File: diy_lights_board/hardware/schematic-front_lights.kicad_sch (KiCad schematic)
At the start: 21 parts, among them Q1 BSP171, Q2 BSP171, Q3 BSP171, Q4 BSP171, Q5 FDV301, Q6 FDV301, Q7 FDV301, Q8 FDV301, Q9 FDV301, U1 Step-down converter to 3.3V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

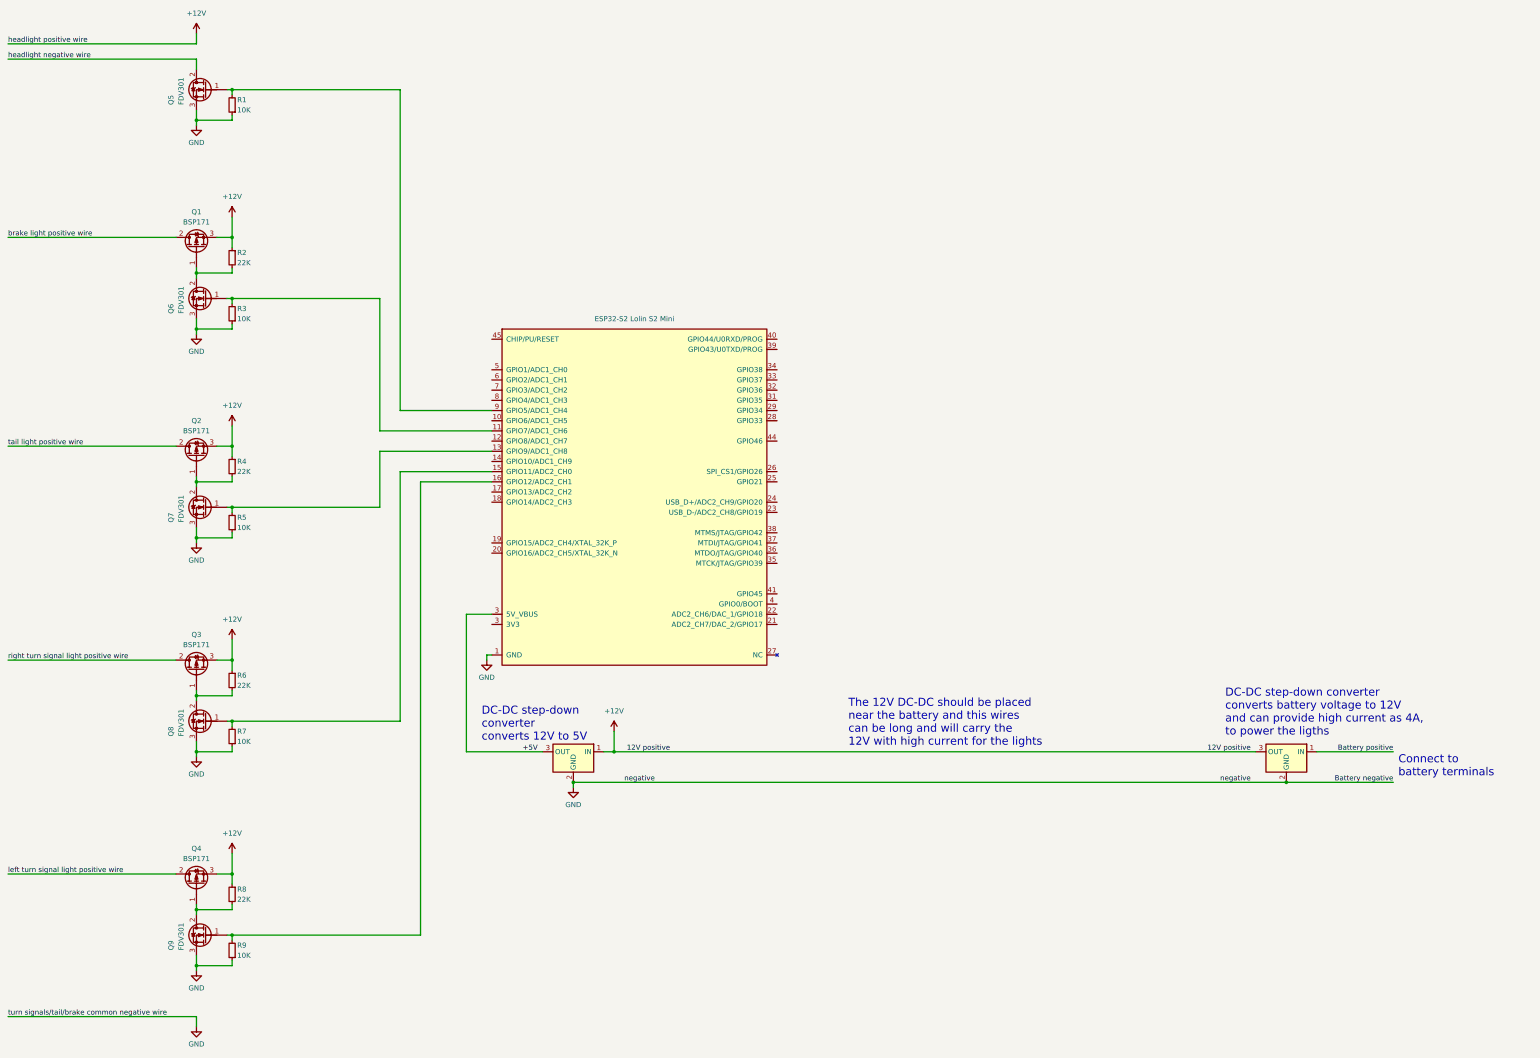
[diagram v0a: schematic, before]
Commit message: Did finish the front and rear lights boards
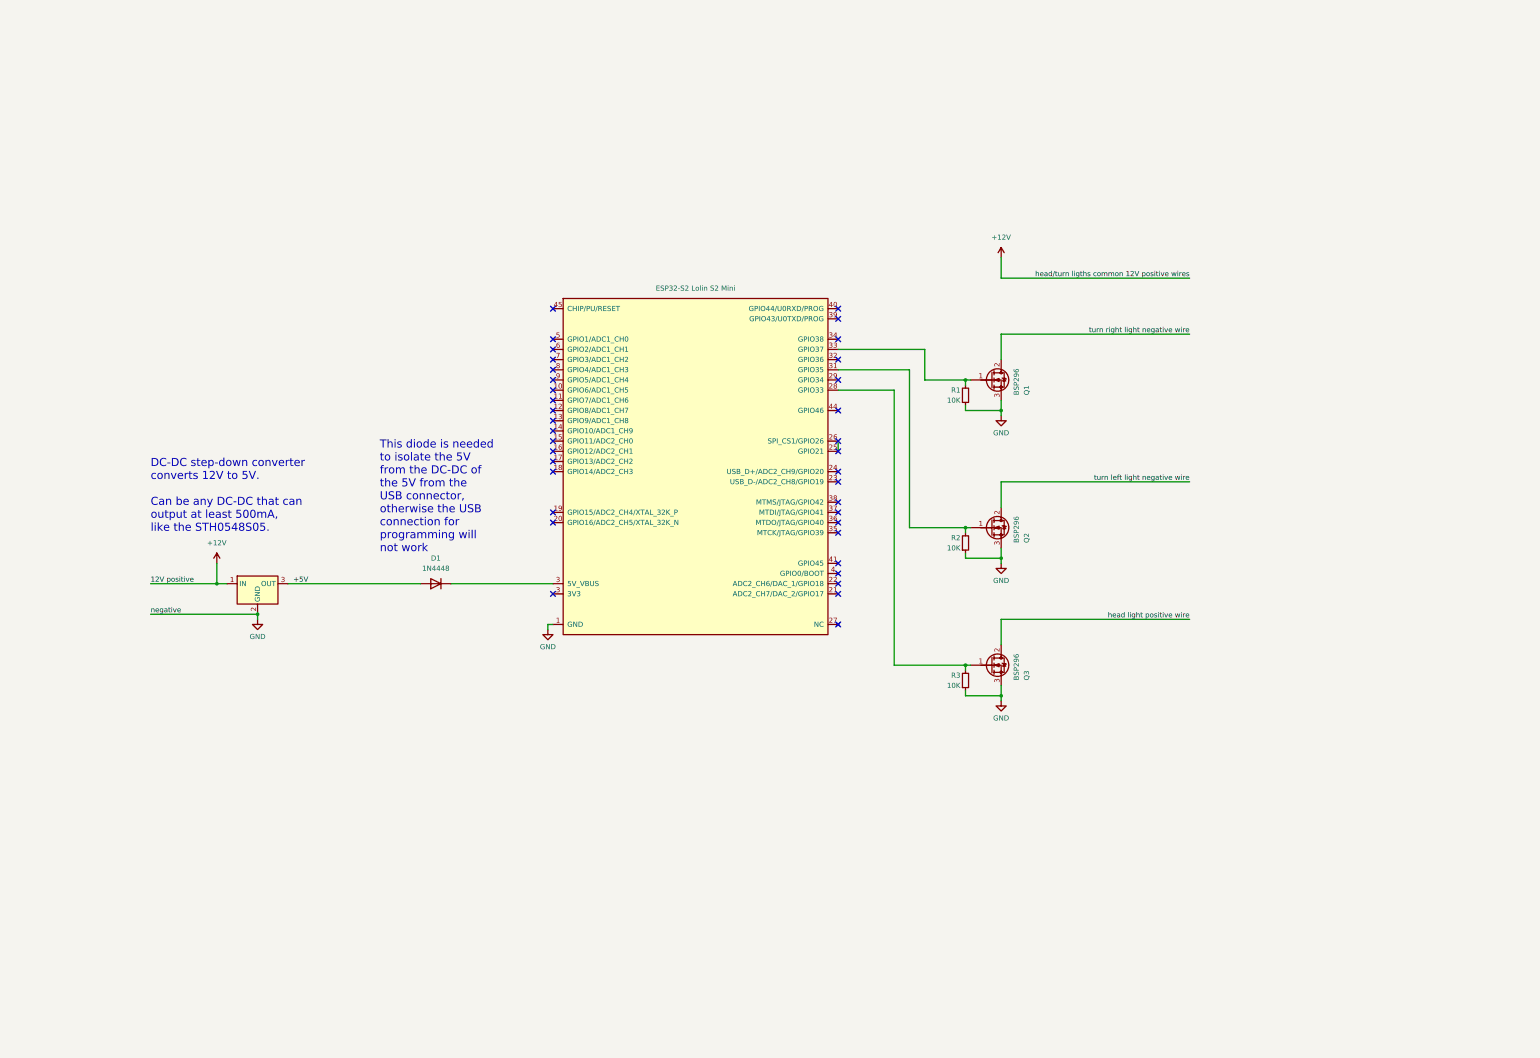
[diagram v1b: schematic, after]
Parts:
- removed Q1, Q2, Q3, Q4: BSP171, Package_TO_SOT_THT:TO-220-3_Vertical, symbol Transistor_FET:IRF9540N
- removed Q5, Q6, Q7, Q8, Q9: FDV301, Package_TO_SOT_SMD:SOT-223-3_TabPin2, symbol Transistor_FET:BSP129
- removed R4, R6, R8: 22K, symbol Device:R_Small
- removed R5, R7, R9: 10K, symbol Device:R_Small
- removed U3: Step-down converter to 3.3V, Converter_DCDC:Converter_DCDC_Murata_OKI-78SR_Vertical, symbol Converter_DCDC:OKI-78SR-3.3_1.5-W36-C
- added D1: 1N4448, Diode_THT:D_DO-35_SOD27_P7.62mm_Horizontal, symbol Diode:1N4448
- added Q1, Q2, Q3: BSP296, Package_TO_SOT_SMD:SOT-223-3_TabPin2, symbol Transistor_FET:BSP129
- R2: value 22K -> 10K
- renumbered U2 to U1, U1 to U2
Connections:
- net +12V: no longer R2.1
- net +5V: now also D1.2 (A); no longer U1.3 (5V_VBUS)
- net GND: now also R2.1, Q1.3 (S), Q2.3 (S), Q3.3 (S)
- net at R3.2: now also U1.28 (GPIO33), Q3.1 (G); no longer U1.11 (GPIO7/ADC1_CH6)
- net at R1.2: now also U1.33 (GPIO37), Q1.1 (G); no longer U1.9 (GPIO5/ADC1_CH4)
- net at R2.2: now also U1.31 (GPIO35), Q2.1 (G)
- net at U1.25 (GPIO21): now also U1.26 (SPI_CS1/GPIO26)
- net at U1.3 (5V_VBUS): now also D1.1 (K)
- new net head light positive wire: Q3.2 (D)
- new net turn left light negative wire: Q2.2 (D)
- new net turn right light negative wire: Q1.2 (D)
- no-connect marks 0 -> 37
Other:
- note added: "DC-DC step-down converter converts 12V to 5V. Can be any DC-DC that can output at least 500mA, like the STH0548S05."
- note added: "This diode is needed to isolate the 5V from the DC-DC of the 5V from the USB connector, otherwise the USB connection for programming will not work"
- note removed: "Connect to battery terminals"
- note removed: "DC-DC step-down converter converts 12V to 5V"
- note removed: "DC-DC step-down converter converts battery voltage to 12V and can provide high current as 4A, to power the ligths"
- note removed: "The 12V DC-DC should be placed near the battery and this wires can be long and will carry the 12V with high current for the lights"
